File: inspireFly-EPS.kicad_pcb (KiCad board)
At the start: 4 copper layers, 88 x 94.5 mm, 62 parts, among them J1 USB4085-GF-A_REVB, J2 Conn_01x02_Pin, Q10 SQJA62EP-T1_GE3, Q3 SQJA62EP-T1_GE3, Q4 SQJA62EP-T1_GE3, Q5 SQJA62EP-T1_GE3, Q6 SQJA62EP-T1_GE3, Q7 SQJA62EP-T1_GE3, Q8 SQJA62EP-T1_GE3, Q9 SQJA62EP-T1_GE3, U1 STM32U575RIT6, U2 BQ25750RRVR, U3 TCAN332DCNR

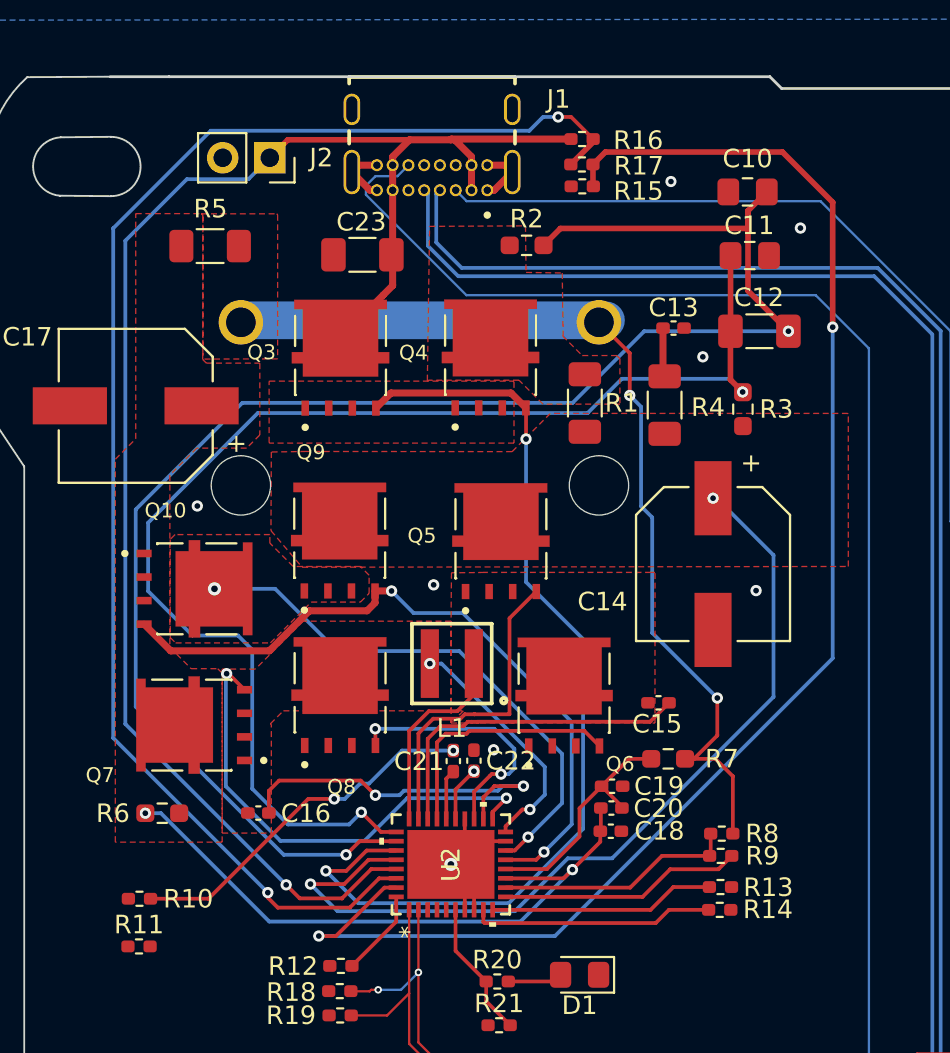
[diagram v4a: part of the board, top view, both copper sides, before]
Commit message: Added diode to USB
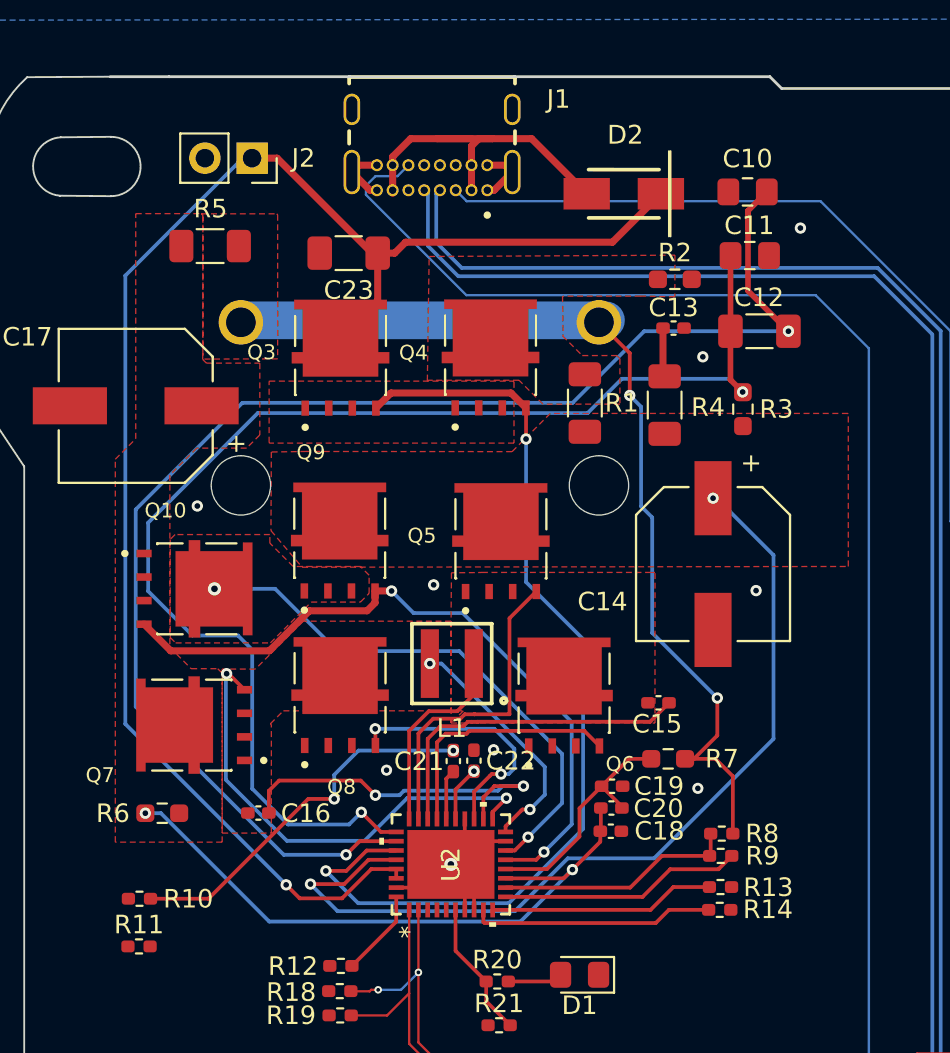
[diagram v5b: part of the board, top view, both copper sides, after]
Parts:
- removed R15: 22.6k, Resistor_SMD:R_0402_1005Metric_Pad0.72x0.64mm_HandSolder
- removed R16: 1M, Resistor_SMD:R_0402_1005Metric_Pad0.72x0.64mm_HandSolder
- removed R17: 100k, Resistor_SMD:R_0402_1005Metric_Pad0.72x0.64mm_HandSolder
- added D2: D_Schottky, inspireFly-EPS-footprints:SDT5A60SA13, F.Cu at (72.3, 31.3)
- moved R2 8.20 mm to (75.1, 35.9)
- moved J2 0.96 mm to (52.3, 29.4)
- moved C23 0.75 mm to (57.5, 34.5)
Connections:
- C23 pad 1: USB_V -> V_BUS_COMBINED
- J2 pad 1: USB_V -> V_BUS_COMBINED
- Q3 pad 1: USB_V -> V_BUS_COMBINED
- U2 pad 33: USB_V -> V_BUS_COMBINED
- U2 pad 34: Net-(U2-ACUV) -> V_BUS_COMBINED
- U2 pad 35: Net-(U2-ACOV) -> BAT -
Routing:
- net V_BUS_COMBINED: track 0.00 -> 84.9 mm, vias 0 -> 1
- net Net-(U2-ACOV): track 79.2 -> 0.00 mm, vias 2 -> 0
- net Net-(U2-ACUV): track 78.1 -> 0.00 mm, vias 2 -> 0
- net USB_V: track 87.0 -> 19.6 mm, vias 1 -> 0
- net Net-(U2-ACP): track 88.6 -> 77.2 mm
- net BAT -: track 37.8 -> 41.2 mm, vias 8 -> 9
- net V_PROTECTED: track 47.6 -> 49.0 mm
- net REGEN: track 19.6 -> 20.4 mm

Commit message: Slight Routing updates
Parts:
- moved C9 12.5 mm to (97.6, 91.0)
- moved U3 11.5 mm to (102.1, 90.2)
- moved TR1 11.5 mm to (106.5, 90.8)
- moved C3 0.93 mm to (74.6, 83.4)
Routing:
- net CAN_RX: track 0.00 -> 39.0 mm
- net CAN_TX: track 0.00 -> 33.0 mm
- net BAT -: track 41.2 -> 52.9 mm, vias 9 -> 13
- net +3.3V: track 23.0 -> 25.2 mm
- net USB_CC2: track 89.6 -> 90.2 mm

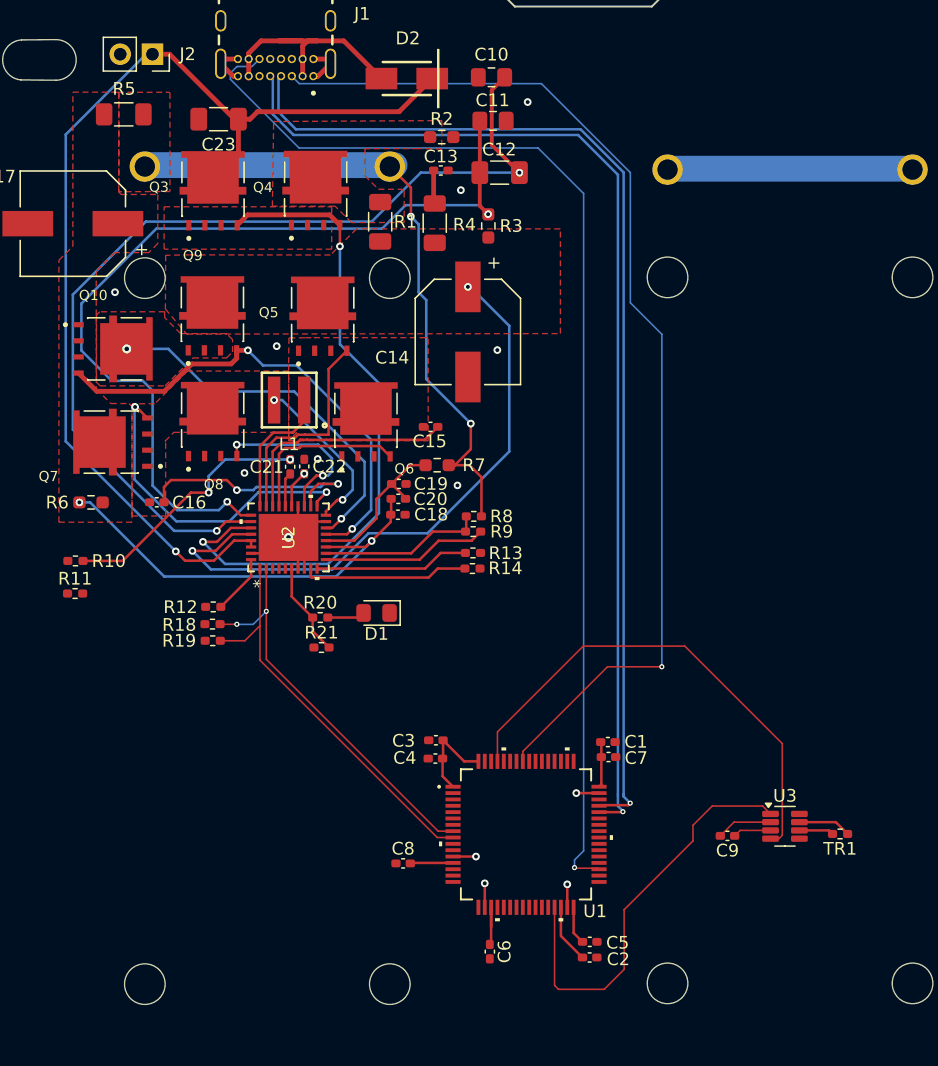
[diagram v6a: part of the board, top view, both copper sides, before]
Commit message: Schematic additions, some routing changes
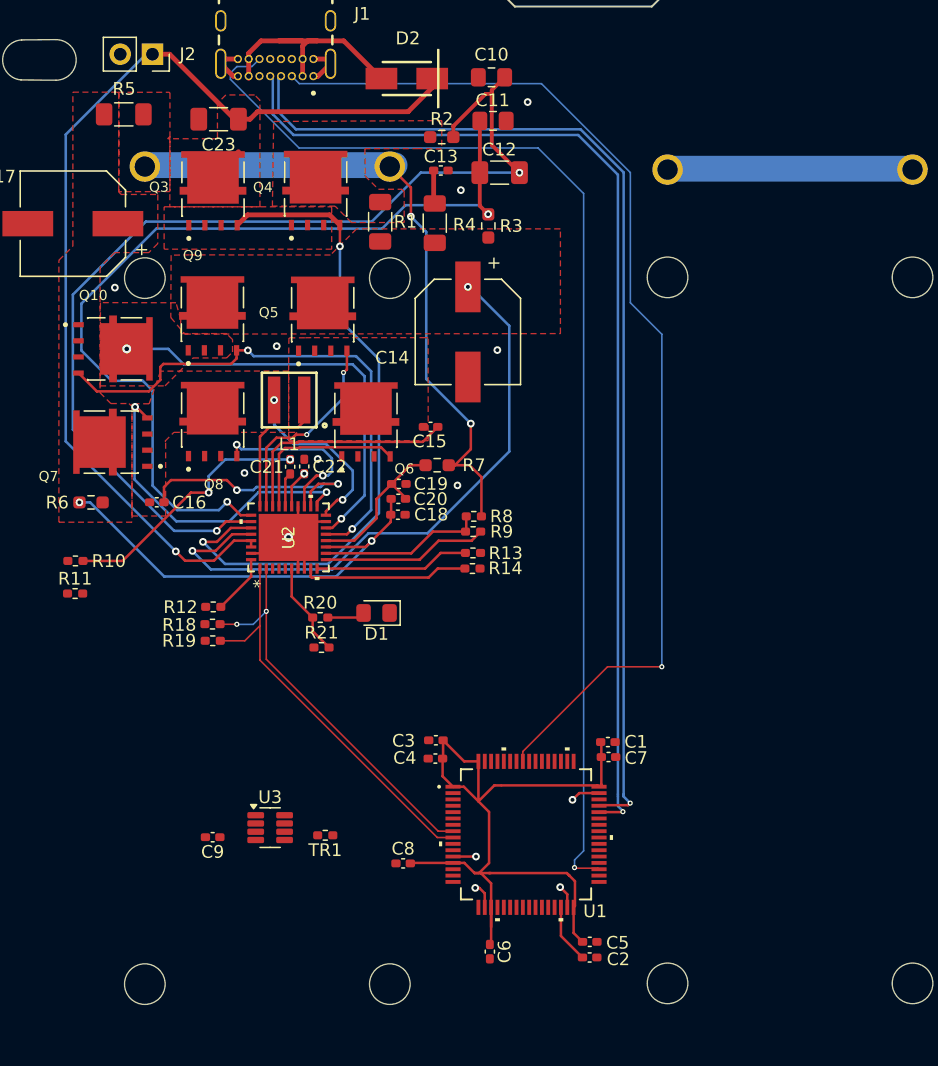
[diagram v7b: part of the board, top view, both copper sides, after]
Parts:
- moved TR1 40.6 mm to (65.9, 90.9)
- moved U3 40.6 mm to (61.5, 90.3)
- moved C9 40.6 mm to (57.0, 91.1)
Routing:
- net CAN_RX: track 39.0 -> 0.00 mm
- net +3.3V: track 25.2 -> 60.1 mm
- net CAN_TX: track 33.0 -> 0.00 mm
- net Net-(U2-ACP): track 77.2 -> 82.2 mm
- net CAN_H: track 4.19 -> 0.00 mm
- net Net-(Q10-D): track 29.2 -> 33.1 mm
- net Net-(Q10-G): track 38.2 -> 41.9 mm
- net BAT -: track 52.9 -> 49.2 mm
- net CAN_L: track 2.72 -> 0.00 mm
- net V_BUS_COMBINED: track 84.9 -> 82.8 mm
- net Net-(Q7-S): track 13.1 -> 14.3 mm
- net Net-(Q5-G): track 17.2 -> 16.2 mm, vias 0 -> 2
- added copper zone on F.Cu, net V_BUS_COMBINED

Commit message: Routing fixes
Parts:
- added C24: 100nF, Capacitor_SMD:C_0402_1005Metric_Pad0.74x0.62mm_HandSolder, F.Cu at (150.2, 61.7)
- added C25: 100nF, Capacitor_SMD:C_0402_1005Metric_Pad0.74x0.62mm_HandSolder, F.Cu at (150.2, 63.7)
- added C26: 100nF, Capacitor_SMD:C_0402_1005Metric_Pad0.74x0.62mm_HandSolder, F.Cu at (150.2, 65.6)
- added C27: 100nF, Capacitor_SMD:C_0402_1005Metric_Pad0.74x0.62mm_HandSolder, F.Cu at (150.2, 67.6)
- added C28: 100nF, Capacitor_SMD:C_0402_1005Metric_Pad0.74x0.62mm_HandSolder, F.Cu at (150.2, 69.6)
- added C29: 100nF, Capacitor_SMD:C_0402_1005Metric_Pad0.74x0.62mm_HandSolder, F.Cu at (150.2, 71.5)
- added C39: 100nF, Capacitor_SMD:C_0805_2012Metric_Pad1.18x1.45mm_HandSolder, F.Cu at (154.2, 78.9)
- added L2: 1.5uH, inspireFly-EPS-footprints:WE-MAPI_4020, F.Cu at (155.3, 63.6)
- added L3: 1.5uH, inspireFly-EPS-footprints:WE-MAPI_4020, F.Cu at (155.3, 69.4)
- added R15: 5m, Resistor_SMD:R_1206_3216Metric_Pad1.30x1.75mm_HandSolder, F.Cu at (161.2, 62.4)
- added R16: 5m, Resistor_SMD:R_1206_3216Metric_Pad1.30x1.75mm_HandSolder, F.Cu at (161.2, 65.7)
- added R17: 10, Resistor_SMD:R_0603_1608Metric_Pad0.98x0.95mm_HandSolder, F.Cu at (145.0, 75.3)
- added R22: 10, Resistor_SMD:R_0603_1608Metric_Pad0.98x0.95mm_HandSolder, F.Cu at (145.0, 77.8)
- added R23: 5m, Resistor_SMD:R_1206_3216Metric_Pad1.30x1.75mm_HandSolder, F.Cu at (161.2, 68.9)
- added R24: 10, Resistor_SMD:R_0603_1608Metric_Pad0.98x0.95mm_HandSolder, F.Cu at (145.0, 80.3)
- added U5: INA180A3IDBVT, inspireFly-EPS-footprints:SOT95P280X145-5N, F.Cu at (146.0, 62.9)
- added U6: INA180A3IDBVT, inspireFly-EPS-footprints:SOT95P280X145-5N, F.Cu at (146.0, 67.4)
- added U7: INA180A3IDBVT, inspireFly-EPS-footprints:SOT95P280X145-5N, F.Cu at (146.0, 71.8)
- added U8: TPS63070RNMR, inspireFly-EPS-footprints:VREG_TPS63070RNMR, F.Cu at (154.5, 74.8)
- added U9: TPS63070RNMR, inspireFly-EPS-footprints:VREG_TPS63070RNMR, F.Cu at (159.5, 74.8)
- C13: footprint Capacitor_SMD:C_0402_1005Metric_Pad0.74x0.62mm_HandSolder -> Capacitor_SMD:C_1206_3216Metric_Pad1.33x1.80mm_HandSolder
- D2: value D_Schottky -> SDT5A60SA
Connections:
- U1 pad 10: unconnected-(U1A-PC2-Pad10) -> ADC1_IN3
- U1 pad 11: unconnected-(U1A-PC3-Pad11) -> ADC1_IN4
- U1 pad 14: unconnected-(U1A-PA0-Pad14) -> ADC1_IN5
- U2 pad 1: I2C3-SDA -> I2C3-SCL
- U2 pad 2: I2C3-SCL -> I2C3-SDA
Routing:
- net I2C3-SDA: track 31.8 -> 33.0 mm
- net I2C3-SCL: track 31.5 -> 32.4 mm
